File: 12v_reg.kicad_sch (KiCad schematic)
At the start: 10 parts, among them U2 SiC467

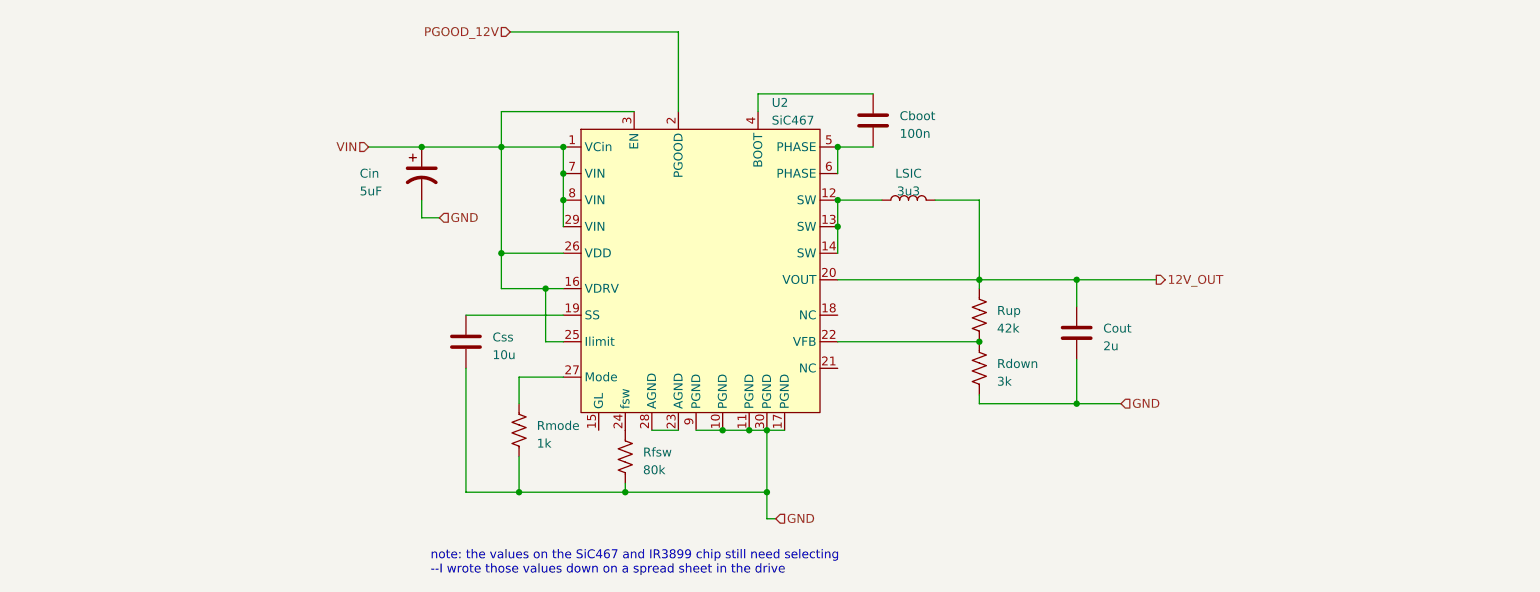
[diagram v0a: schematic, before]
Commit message: Changed 12V Regulator values, added thruster side 3V3 regulator
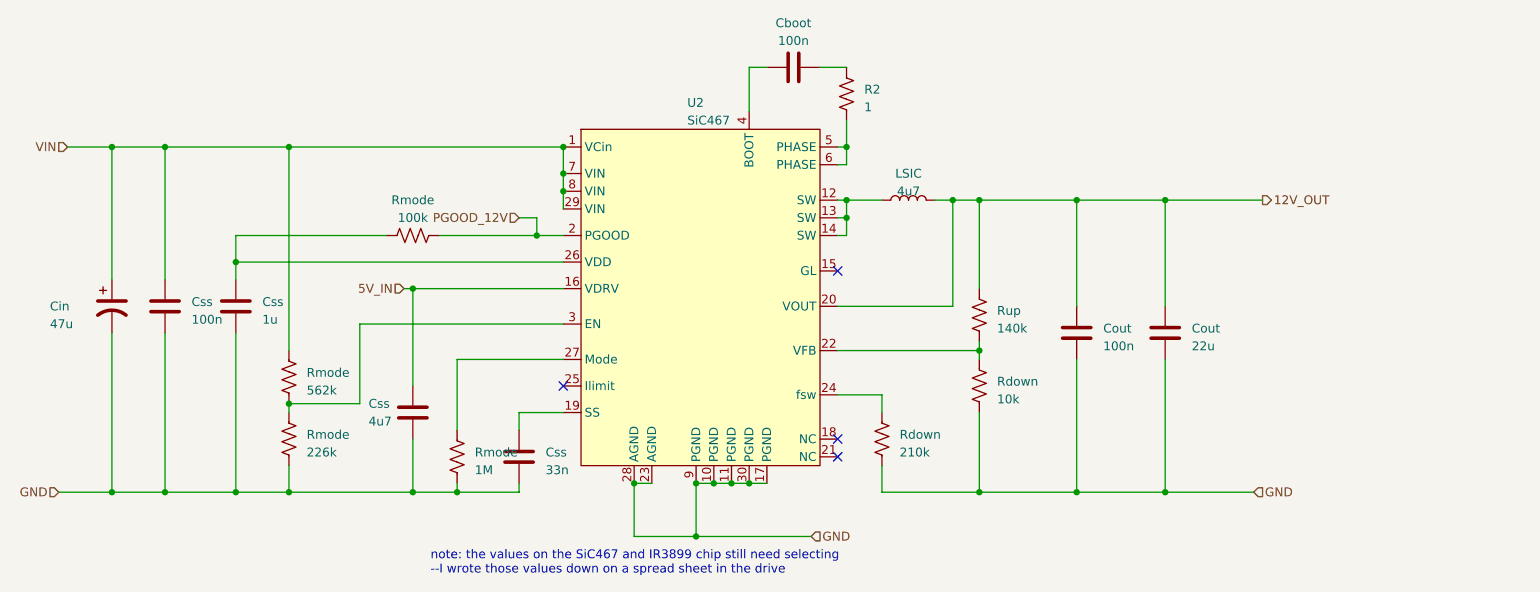
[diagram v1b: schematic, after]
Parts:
- removed Rfsw: 80k, symbol Device:R_US
- added Cout: 22u, symbol Device:C
- added Css: 100n, symbol Device:C
- added Css: 1u, symbol Device:C
- added Css: 4u7, symbol Device:C
- added R2: 1, symbol Device:R_US
- added Rdown: 210k, symbol Device:R_US
- added Rmode: 100k, symbol Device:R_US
- added Rmode: 226k, symbol Device:R_US
- added Rmode: 562k, symbol Device:R_US
- Cin: value 5uF -> 47u
- Cout: value 2u -> 100n
- Css: value 10u -> 33n
- LSIC: value 3u3 -> 4u7
- Rdown: value 3k -> 10k
- Rmode: value 1k -> 1M
- Rup: value 42k -> 140k
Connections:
- net 12V_OUT: now also Cout.1
- net GND: now also Css.1, U2.23 (AGND), U2.28 (AGND), Cout.2, Css.1, Css.1, Css.1, Rdown.2, Rmode.1; no longer Css.2
- net PGOOD_12V: now also Rmode.2
- net VIN: now also Css.2, Rmode.2; no longer U2.16 (VDRV), U2.25 (Ilimit), U2.26 (VDD), U2.3 (EN)
- net at U2.19 (SS): now also Css.2; no longer Css.1
- net at U2.5 (PHASE), U2.6 (PHASE): now also R2.1; no longer Cboot.2
- net at U2.24 (fsw): now also Rdown.1
- new net: Cboot.2, R2.2
- new net: Css.2, Rmode.1, U2.26 (VDD)
- new net: Rmode.1, Rmode.2, U2.3 (EN)
- new net 5V_IN: Css.2, U2.16 (VDRV)
- no-connect marks 0 -> 4
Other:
- moved on the sheet: Cboot, Cin, Css, Rdown, Rmode, U2

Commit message: Added extra output capacitance to 12V regulator, added component designators
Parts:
- added Cout: 22u, symbol Device:C
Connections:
- net 12V_OUT: now also Cout.1
- net GND: now also Cout.2
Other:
- note removed: "note: the values on the SiC467 and IR3899 chip still need selecting --I wrote those values down on a spread sheet in the drive"
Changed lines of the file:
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@@
 (kicad_sch (version 20230121) (generator eeschema)
   (paper "A4")
+  (junction (at 212.09 111.76) (diameter 0) (color 0 0 0 0)
+  )
   (junction (at 114.3 62.23) (diameter 0) (color 0 0 0 0)
   )
@@
   )
   (junction (at 135.89 110.49) (diameter 0) (color 0 0 0 0)
+  )
+  (junction (at 212.09 69.85) (diameter 0) (color 0 0 0 0)
   )
   (junction (at 154.94 69.85) (diameter 0) (color 0 0 0 0)
@@
   (no_connect (at 153.67 80.01))
   (no_connect (at 153.67 104.14))
+  (wire (pts (xy 212.09 69.85) (xy 214.63 69.85))
+    (stroke (width 0) (type default))
+  )
+  (wire (pts (xy 212.09 111.76) (xy 213.36 111.76))
+    (stroke (width 0) (type default))
+  )
   (wire (pts (xy 74.93 107.95) (xy 74.93 111.76))
     (stroke (width 0) (type default))
@@
     (stroke (width 0) (type default))
   )
-  (wire (pts (xy 200.66 69.85) (xy 214.63 69.85))
+  (wire (pts (xy 200.66 69.85) (xy 212.09 69.85))
     (stroke (width 0) (type default))
   )
@@
     (stroke (width 0) (type default))
   )
-  (wire (pts (xy 200.66 111.76) (xy 213.36 111.76))
+  (wire (pts (xy 200.66 111.76) (xy 212.09 111.76))
     (stroke (width 0) (type default))
   )
@@
     (stroke (width 0) (type default))
   )
+  (wire (pts (xy 212.09 92.71) (xy 212.09 111.76))
+    (stroke (width 0) (type default))
+  )
   (wire (pts (xy 88.9 74.93) (xy 67.31 74.93))
     (stroke (width 0) (type default))
   )
+  (wire (pts (xy 212.09 69.85) (xy 212.09 85.09))
+    (stroke (width 0) (type default))
+  )
   (wire (pts (xy 170.18 85.09) (xy 170.18 69.85))
     (stroke (width 0) (type default))
@@
   (wire (pts (xy 67.31 74.93) (xy 67.31 78.74))
     (stroke (width 0) (type default))
-  )
-  (text "note: the values on the SiC467 and IR3899 chip still need selecting\n--I wrote those values down on a spread sheet in the drive\n\n"
-    (at 95.25 125.73 0)
-    (effects (font (size 1.27 1.27)) (justify left bottom))
   )
   (hierarchical_label "GND" (shape input) (at 41.91 111.76 180) (fields_autoplaced)
@@
         )
       )
+    )
+  )
+  (symbol (lib_id "Device:C") (at 212.09 88.9 0) (unit 1)
+    (in_bom yes) (on_board yes) (dnp no) (fields_autoplaced)
+    (property "Reference" "Cout" (at 215.9 88.265 0)
+      (effects (font (size 1.27 1.27)) (justify left))
+    )
+    (property "Value" "22u" (at 215.9 90.805 0)
+      (effects (font (size 1.27 1.27)) (justify left))
+    )
+    (property "Footprint" "" (at 213.0552 92.71 0)
+      (effects (font (size 1.27 1.27)) hide)
+    )
+    (property "Datasheet" "~" (at 212.09 88.9 0)
+      (effects (font (size 1.27 1.27)) hide)
+    )
+    (pin "1")
+    (pin "2")
+    (instances
+      (project "crush-power-board"
+        (path "/530b9f5d-4c5f-47a4-a889-3cce870d311f"
+          (reference "Cout") (unit 1)
+        )
+        (path "/530b9f5d-4c5f-47a4-a889-3cce870d311f/8fa80497-01bc-4617-b4f1-76ea41313a51"
+          (reference "C17") (unit 1)
+        )
+      )

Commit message: Added more component footprints
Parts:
- U2: footprint (none) -> crush-power-footprints:SIC467ED-T1-GE3
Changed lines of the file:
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@@
       (effects (font (size 1.27 1.27)) (justify left))
     )
-    (property "Footprint" "" (at 125.73 69.85 0)
+    (property "Footprint" "crush-power-footprints:SIC467ED-T1-GE3" (at 125.73 69.85 0)
       (effects (font (size 1.27 1.27)) hide)
     )
-    (property "Datasheet" "" (at 125.73 69.85 0)
+    (property "Datasheet" "https://www.vishay.com/docs/76044/sic46x.pdf" (at 125.73 69.85 0)
       (effects (font (size 1.27 1.27)) hide)
     )

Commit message: Fixed a lot of components
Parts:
- added Cout (x2): 22u, Capacitor_SMD:C_1210_3225Metric_Pad1.33x2.70mm_HandSolder, symbol Device:C
- Cboot, Cout, Css: footprint (none) -> Capacitor_SMD:C_0603_1608Metric
- Cin: footprint (none) -> Capacitor_Tantalum_SMD:CP_EIA-7343-15_Kemet-W_Pad2.25x2.55mm_HandSolder
- Cout: footprint (none) -> Capacitor_SMD:C_1210_3225Metric_Pad1.33x2.70mm_HandSolder
- LSIC: footprint (none) -> crush-power-footprints:IND_IHLP-6767GZ_VIS-M
- R2: value 1 -> 1R; footprint (none) -> Resistor_SMD:R_0201_0603Metric
- Rdown, Rmode, Rup: footprint (none) -> Resistor_SMD:R_0201_0603Metric
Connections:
- net 12V_OUT: now also Cout.1, Cout.1
- net GND: now also Cout.2, Cout.2
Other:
- moved on the sheet: Cout

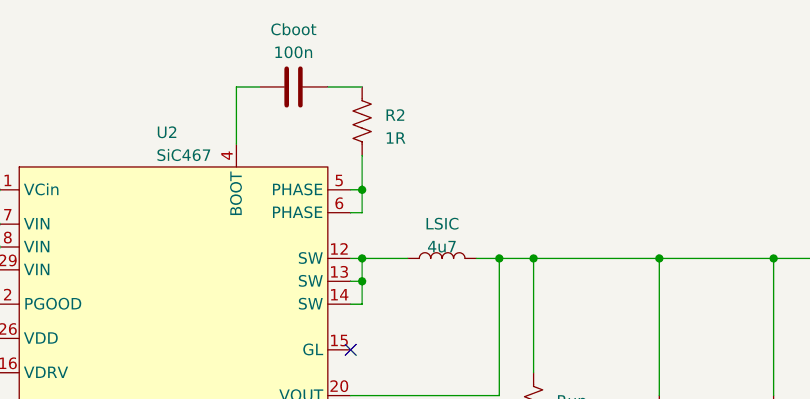
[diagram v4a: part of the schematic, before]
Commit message: Fixed reference designators
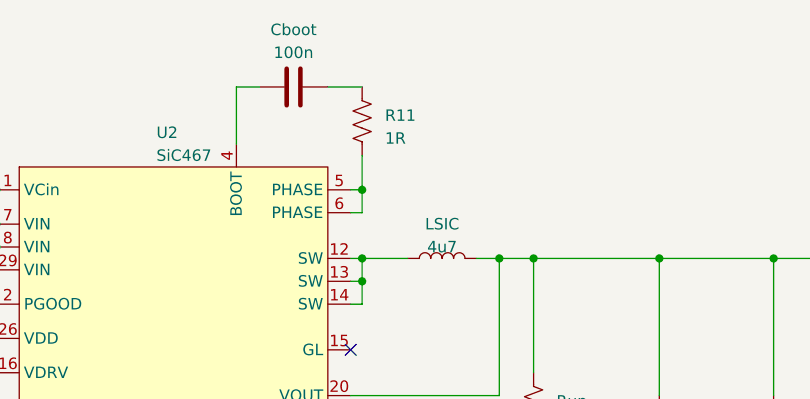
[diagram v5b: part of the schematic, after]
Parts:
- renumbered R2 to R11
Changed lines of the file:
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@@
   (symbol (lib_id "Device:R_US") (at 154.94 54.61 180) (unit 1)
     (in_bom yes) (on_board yes) (dnp no) (fields_autoplaced)
-    (property "Reference" "R2" (at 157.48 53.975 0)
+    (property "Reference" "R11" (at 157.48 53.975 0)
       (effects (font (size 1.27 1.27)) (justify right))
     )
@@
       (project "crush-power-board"
         (path "/530b9f5d-4c5f-47a4-a889-3cce870d311f/8fa80497-01bc-4617-b4f1-76ea41313a51"
-          (reference "R2") (unit 1)
+          (reference "R11") (unit 1)
         )
       )
@@
         )
         (path "/530b9f5d-4c5f-47a4-a889-3cce870d311f/8fa80497-01bc-4617-b4f1-76ea41313a51"
-          (reference "Cout1") (unit 1)
+          (reference "C13") (unit 1)
         )
       )
@@
         )
         (path "/530b9f5d-4c5f-47a4-a889-3cce870d311f/8fa80497-01bc-4617-b4f1-76ea41313a51"
-          (reference "C17") (unit 1)
+          (reference "C15") (unit 1)
         )
       )
@@
         )
         (path "/530b9f5d-4c5f-47a4-a889-3cce870d311f/8fa80497-01bc-4617-b4f1-76ea41313a51"
-          (reference "C11") (unit 1)
+          (reference "C12") (unit 1)
         )
       )
@@
         )
         (path "/530b9f5d-4c5f-47a4-a889-3cce870d311f/8fa80497-01bc-4617-b4f1-76ea41313a51"
-          (reference "C12") (unit 1)
+          (reference "C10") (unit 1)
         )
       )
@@
         )
         (path "/530b9f5d-4c5f-47a4-a889-3cce870d311f/8fa80497-01bc-4617-b4f1-76ea41313a51"
-          (reference "C10") (unit 1)
+          (reference "C11") (unit 1)
         )
       )
@@
         )
         (path "/530b9f5d-4c5f-47a4-a889-3cce870d311f/8fa80497-01bc-4617-b4f1-76ea41313a51"
-          (reference "R11") (unit 1)
+          (reference "R9") (unit 1)
         )
       )
@@
         )
         (path "/530b9f5d-4c5f-47a4-a889-3cce870d311f/8fa80497-01bc-4617-b4f1-76ea41313a51"
-          (reference "C2") (unit 1)
+          (reference "C6") (unit 1)
         )
       )
@@
         )
         (path "/530b9f5d-4c5f-47a4-a889-3cce870d311f/8fa80497-01bc-4617-b4f1-76ea41313a51"
-          (reference "U1") (unit 1)
+          (reference "U2") (unit 1)
         )
       )
@@
         )
         (path "/530b9f5d-4c5f-47a4-a889-3cce870d311f/8fa80497-01bc-4617-b4f1-76ea41313a51"
-          (reference "R12") (unit 1)
+          (reference "R10") (unit 1)
         )
       )
@@
         )
         (path "/530b9f5d-4c5f-47a4-a889-3cce870d311f/8fa80497-01bc-4617-b4f1-76ea41313a51"
-          (reference "R15") (unit 1)
+          (reference "R14") (unit 1)
         )
       )
@@
         )
         (path "/530b9f5d-4c5f-47a4-a889-3cce870d311f/8fa80497-01bc-4617-b4f1-76ea41313a51"
-          (reference "Cout2") (unit 1)
+          (reference "C14") (unit 1)
         )
       )
@@
         )
         (path "/530b9f5d-4c5f-47a4-a889-3cce870d311f/8fa80497-01bc-4617-b4f1-76ea41313a51"
-          (reference "C1") (unit 1)
+          (reference "C5") (unit 1)
         )
       )
@@
         )
         (path "/530b9f5d-4c5f-47a4-a889-3cce870d311f/8fa80497-01bc-4617-b4f1-76ea41313a51"
-          (reference "R10") (unit 1)
+          (reference "R8") (unit 1)
         )
       )
@@
         )
         (path "/530b9f5d-4c5f-47a4-a889-3cce870d311f/8fa80497-01bc-4617-b4f1-76ea41313a51"
-          (reference "R13") (unit 1)
+          (reference "R12") (unit 1)
         )
       )
@@
         )
         (path "/530b9f5d-4c5f-47a4-a889-3cce870d311f/8fa80497-01bc-4617-b4f1-76ea41313a51"
-          (reference "R3") (unit 1)
+          (reference "R7") (unit 1)
         )
       )
@@
         )
         (path "/530b9f5d-4c5f-47a4-a889-3cce870d311f/8fa80497-01bc-4617-b4f1-76ea41313a51"
-          (reference "L1") (unit 1)
+          (reference "L2") (unit 1)
         )
       )
@@
         )
         (path "/530b9f5d-4c5f-47a4-a889-3cce870d311f/8fa80497-01bc-4617-b4f1-76ea41313a51"
-          (reference "R14") (unit 1)
+          (reference "R13") (unit 1)
         )
       )
@@
         )
         (path "/530b9f5d-4c5f-47a4-a889-3cce870d311f/8fa80497-01bc-4617-b4f1-76ea41313a51"
-          (reference "C3") (unit 1)
+          (reference "C7") (unit 1)
         )
       )
@@
         )
         (path "/530b9f5d-4c5f-47a4-a889-3cce870d311f/8fa80497-01bc-4617-b4f1-76ea41313a51"
-          (reference "C4") (unit 1)
-        )
-      )
+          (reference "C8") (unit 1)
+        )
+      )

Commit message: Added indicator LEDs and fixed some footprints
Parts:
- Cin: footprint Capacitor_Tantalum_SMD:CP_EIA-7343-15_Kemet-W_Pad2.25x2.55mm_HandSolder -> Capacitor_Tantalum_SMD:CP_EIA-7343-15_Kemet-W
- Cout: footprint Capacitor_SMD:C_1210_3225Metric_Pad1.33x2.70mm_HandSolder -> Capacitor_SMD:C_1210_3225Metric
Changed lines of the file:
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@@
       (effects (font (size 1.27 1.27)) (justify left))
     )
-    (property "Footprint" "Capacitor_SMD:C_1210_3225Metric_Pad1.33x2.70mm_HandSolder" (at 213.0552 92.71 0)
+    (property "Footprint" "Capacitor_SMD:C_1210_3225Metric" (at 213.0552 92.71 0)
       (effects (font (size 1.27 1.27)) hide)
     )
@@
       (effects (font (size 1.27 1.27)) (justify left))
     )
-    (property "Footprint" "Capacitor_SMD:C_1210_3225Metric_Pad1.33x2.70mm_HandSolder" (at 239.7252 92.71 0)
+    (property "Footprint" "Capacitor_SMD:C_1210_3225Metric" (at 239.7252 92.71 0)
       (effects (font (size 1.27 1.27)) hide)
     )
@@
       (effects (font (size 1.27 1.27)) (justify left))
     )
-    (property "Footprint" "Capacitor_SMD:C_1210_3225Metric_Pad1.33x2.70mm_HandSolder" (at 201.6252 92.71 0)
+    (property "Footprint" "Capacitor_SMD:C_1210_3225Metric" (at 201.6252 92.71 0)
       (effects (font (size 1.27 1.27)) hide)
     )
@@
       (effects (font (size 1.27 1.27)) (justify left))
     )
-    (property "Footprint" "Capacitor_SMD:C_1210_3225Metric_Pad1.33x2.70mm_HandSolder" (at 225.7552 92.71 0)
+    (property "Footprint" "Capacitor_SMD:C_1210_3225Metric" (at 225.7552 92.71 0)
       (effects (font (size 1.27 1.27)) hide)
     )
@@
       (effects (font (size 1.27 1.27)) (justify left))
     )
-    (property "Footprint" "Capacitor_Tantalum_SMD:CP_EIA-7343-15_Kemet-W_Pad2.25x2.55mm_HandSolder" (at 49.53 85.09 0)
-      (effects (font (size 1.27 1.27)) hide)
-    )
+    (property "Footprint" "Capacitor_Tantalum_SMD:CP_EIA-7343-15_Kemet-W" (at 49.53 85.09 0)
+      (effects (font (size 1.27 1.27)) hide)
+    )

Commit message: fixed some more footprints for resistors. 0201 -> 0603
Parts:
- R11, Rdown, Rmode, Rup: footprint Resistor_SMD:R_0201_0603Metric -> Resistor_SMD:R_0603_1608Metric
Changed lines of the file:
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@@
       (effects (font (size 1.27 1.27)) (justify right))
     )
-    (property "Footprint" "Resistor_SMD:R_0201_0603Metric" (at 153.924 54.356 90)
+    (property "Footprint" "Resistor_SMD:R_0603_1608Metric" (at 153.924 54.356 90)
       (effects (font (size 1.27 1.27)) hide)
     )
@@
       (effects (font (size 1.27 1.27)))
     )
-    (property "Footprint" "Resistor_SMD:R_0201_0603Metric" (at 92.964 73.914 90)
+    (property "Footprint" "Resistor_SMD:R_0603_1608Metric" (at 92.964 73.914 90)
       (effects (font (size 1.27 1.27)) hide)
     )
@@
       (effects (font (size 1.27 1.27)) (justify left))
     )
-    (property "Footprint" "Resistor_SMD:R_0201_0603Metric" (at 100.076 106.934 90)
+    (property "Footprint" "Resistor_SMD:R_0603_1608Metric" (at 100.076 106.934 90)
       (effects (font (size 1.27 1.27)) hide)
     )
@@
       (effects (font (size 1.27 1.27)) (justify left))
     )
-    (property "Footprint" "Resistor_SMD:R_0201_0603Metric" (at 175.006 96.774 90)
+    (property "Footprint" "Resistor_SMD:R_0603_1608Metric" (at 175.006 96.774 90)
       (effects (font (size 1.27 1.27)) hide)
     )
@@
       (effects (font (size 1.27 1.27)) (justify right))
     )
-    (property "Footprint" "Resistor_SMD:R_0201_0603Metric" (at 73.914 103.886 90)
+    (property "Footprint" "Resistor_SMD:R_0603_1608Metric" (at 73.914 103.886 90)
       (effects (font (size 1.27 1.27)) hide)
     )
@@
       (effects (font (size 1.27 1.27)) (justify left))
     )
-    (property "Footprint" "Resistor_SMD:R_0201_0603Metric" (at 161.036 104.394 90)
+    (property "Footprint" "Resistor_SMD:R_0603_1608Metric" (at 161.036 104.394 90)
       (effects (font (size 1.27 1.27)) hide)
     )
@@
       (effects (font (size 1.27 1.27)) (justify right))
     )
-    (property "Footprint" "Resistor_SMD:R_0201_0603Metric" (at 73.914 94.996 90)
+    (property "Footprint" "Resistor_SMD:R_0603_1608Metric" (at 73.914 94.996 90)
       (effects (font (size 1.27 1.27)) hide)
     )
@@
       (effects (font (size 1.27 1.27)) (justify left))
     )
-    (property "Footprint" "Resistor_SMD:R_0201_0603Metric" (at 175.006 86.614 90)
-      (effects (font (size 1.27 1.27)) hide)
-    )
+    (property "Footprint" "Resistor_SMD:R_0603_1608Metric" (at 175.006 86.614 90)
+      (effects (font (size 1.27 1.27)) hide)
+    )

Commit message: Changed boot/phase resistor and cap to be 0402 package according to SiC467 datasheet
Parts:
- Cboot: footprint Capacitor_SMD:C_0603_1608Metric -> Capacitor_SMD:C_0402_1005Metric
- R11: footprint Resistor_SMD:R_0603_1608Metric -> Resistor_SMD:R_0402_1005Metric
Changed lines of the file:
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@@
       (effects (font (size 1.27 1.27)) (justify right))
     )
-    (property "Footprint" "Resistor_SMD:R_0603_1608Metric" (at 153.924 54.356 90)
+    (property "Footprint" "Resistor_SMD:R_0402_1005Metric" (at 153.924 54.356 90)
       (effects (font (size 1.27 1.27)) hide)
     )
@@
       (effects (font (size 1.27 1.27)))
     )
-    (property "Footprint" "Capacitor_SMD:C_0603_1608Metric" (at 151.13 49.8348 0)
+    (property "Footprint" "Capacitor_SMD:C_0402_1005Metric" (at 151.13 49.8348 0)
       (effects (font (size 1.27 1.27)) hide)
     )
